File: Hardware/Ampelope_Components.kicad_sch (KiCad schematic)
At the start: 121 parts, among them J1 Conn_01x12_Male, J2 Conn_01x12_Male, J3 Conn_01x12_Male, J4 Conn_01x12_Male, J5 Eurorack_16_pin_power, J6 Conn_01x02_Male, J7 SWD_Header, J8 USB_B_Micro, J9 Conn_01x02_Male, Q1 MMBT3906, Q2 MMBT3906, Q3 MMBT3906, Q4 MMBT3906, Q5 MMBT3906, U1 STM32G431RB, U2 AS3364, U3 LM1117-3.3, U4 TL074, U5 TL074, U6 TL074, Y1 8MHz 20pF

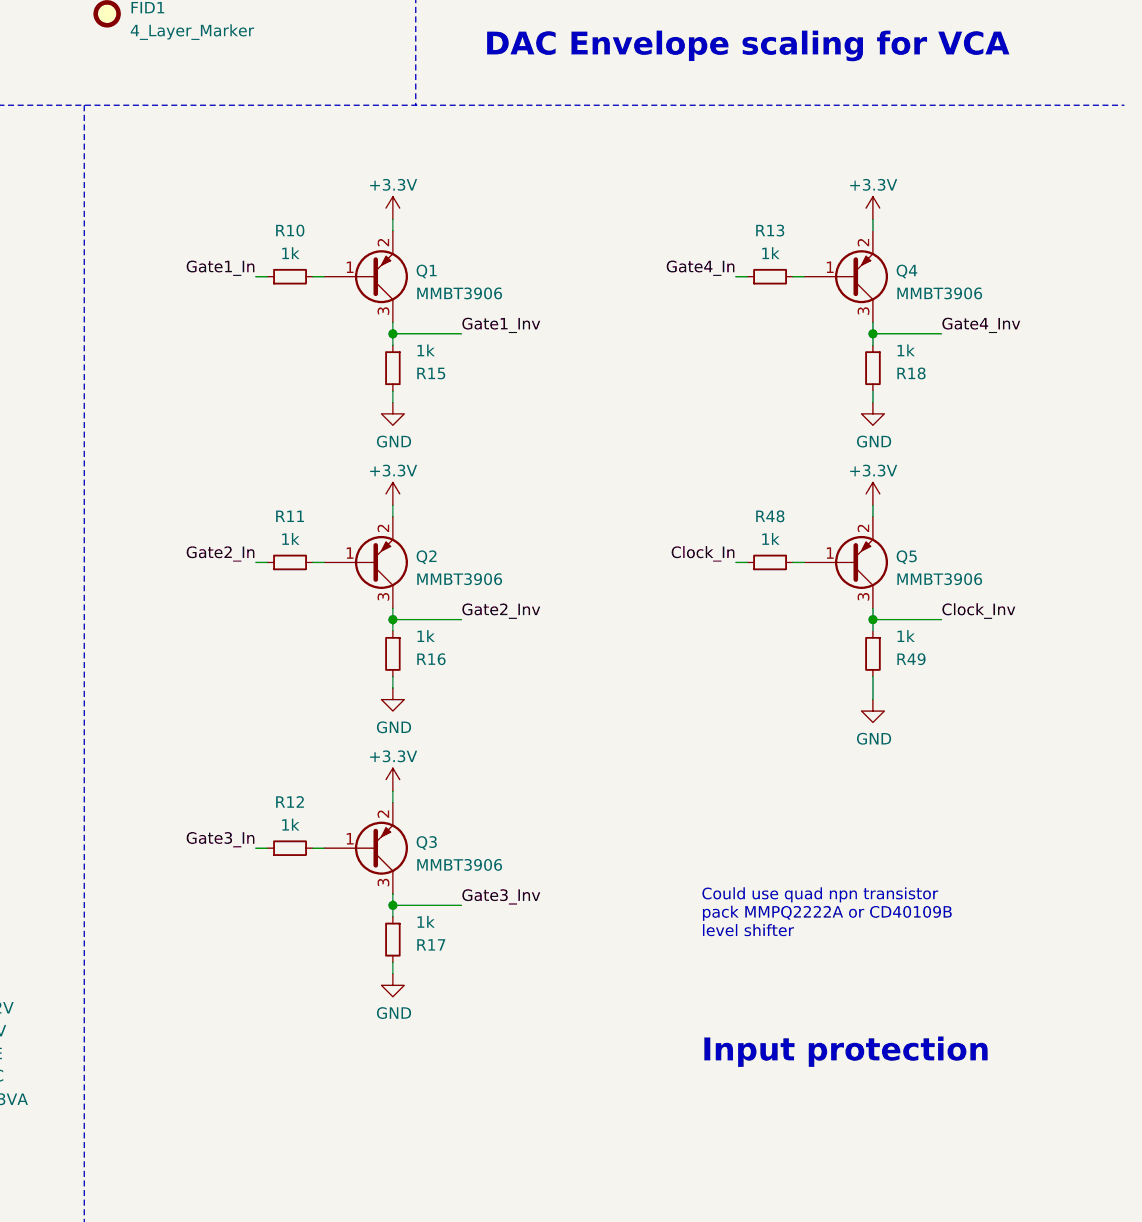
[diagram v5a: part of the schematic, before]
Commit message: Changed input protection diodes back to 3904s; prepared gerbers
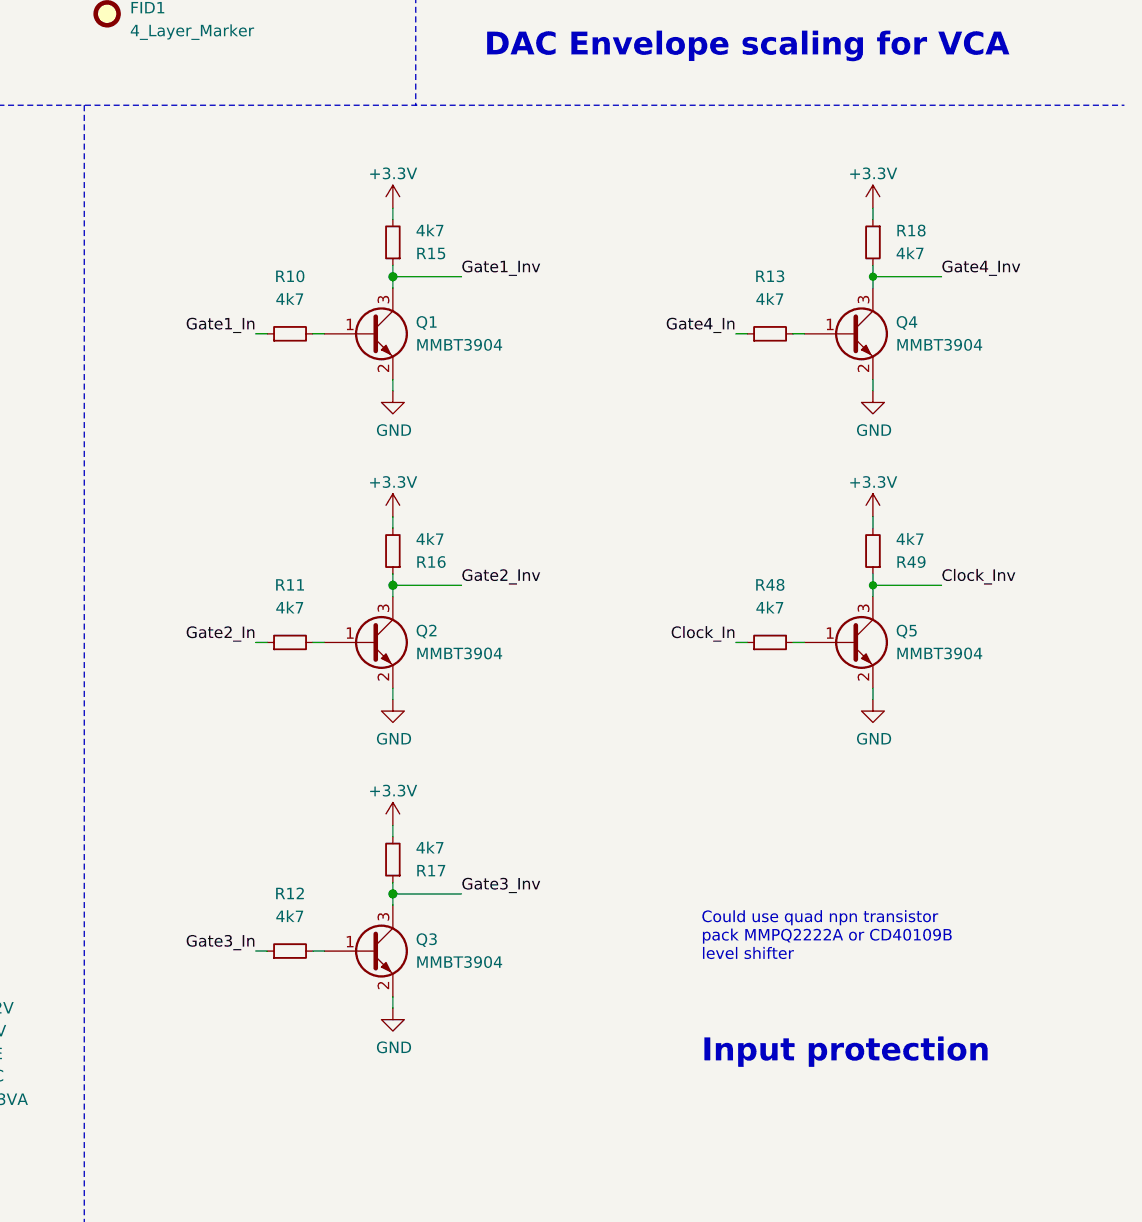
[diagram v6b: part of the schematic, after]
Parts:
- removed Q1, Q2, Q3, Q4, Q5: MMBT3906, Package_TO_SOT_SMD:SOT-23, symbol Transistor_BJT:MMBT3906
- added Q1, Q2, Q3, Q4, Q5: MMBT3904, Package_TO_SOT_SMD:SOT-23, symbol Transistor_BJT:MMBT3904
- C10: Part_Number (none) -> C19666
- C11, C13, C23, C26, C9: Part_Number (none) -> C14663
- C12, C15: Part_Number (none) -> C15849
- C14: Part_Number (none) -> C57112
- C16, C17, C18, C19: Part_Number C84721 -> (none)
- C21, C22: Part_Number C84721 -> C14663
- C24, C25: Part_Number (none) -> C22397
- C27, C28, C29, C30: Part_Number C57112 -> C1604
- C5, C6, C7, C8: Part_Number (none) -> C14858
- L1: Part_Number (none) -> C1046
- R1, R3, R5, R7: Part_Number C22984 -> C21190
- R10, R11, R12, R13, R15, R16, R17, R18, R48, R49: value 1k -> 4k7; Part_Number (none) -> C23162
- R19, R20, R21, R22, R23, R24, R25, R26: Part_Number C22984 -> C25804
- R35, R37, R39, R41: Part_Number (none) -> C23212
- R36, R38, R40, R42: Part_Number C25803 -> C22978
- R43, R44, R45, R46: Part_Number C25819 -> C23162
- R47, R50, R51, R52, R57, R58, R59, R60: Part_Number C25819 -> C21190
- R53, R54, R55, R56: Part_Number (none) -> C25804
- R9: Part_Number (none) -> C25803
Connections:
- net +3V3: now also R15.2, R16.2, R17.2, R18.1, R49.2
- net Clock_Inv: now also Q5.3 (C)
- net GND: now also Q1.2 (E), Q2.2 (E), Q3.2 (E), Q4.2 (E), Q5.2 (E); no longer R15.2, R16.2, R17.2, R18.2, R49.2
- net Gate1_Inv: now also Q1.3 (C)
- net Gate2_Inv: now also Q2.3 (C)
- net Gate3_Inv: now also Q3.3 (C)
- net Gate4_Inv: now also R18.2, Q4.3 (C); no longer R18.1
- net at R12.2: now also Q3.1 (B)
- net at R10.2: now also Q1.1 (B)
- net at R48.2: now also Q5.1 (B)
- net at R11.2: now also Q2.1 (B)
- net at R13.2: now also Q4.1 (B)
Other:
- moved on the sheet: R10, R11, R12, R13, R15, R16, R17, R18, R48, R49

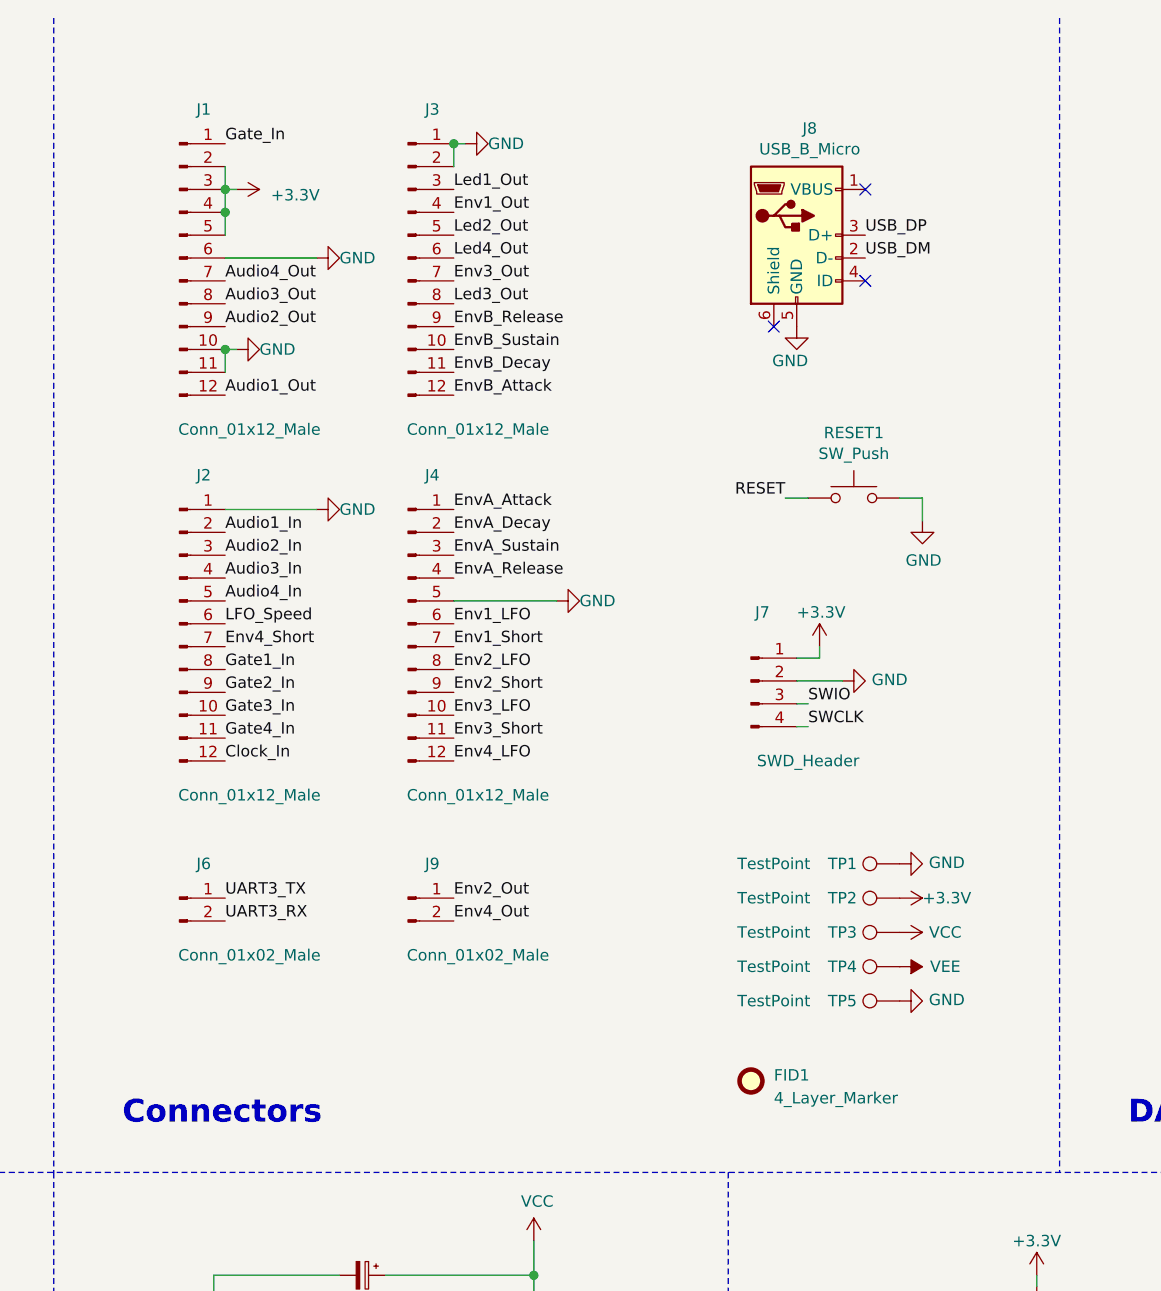
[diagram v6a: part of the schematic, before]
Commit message: Prepared gerbers for pcb manufacture
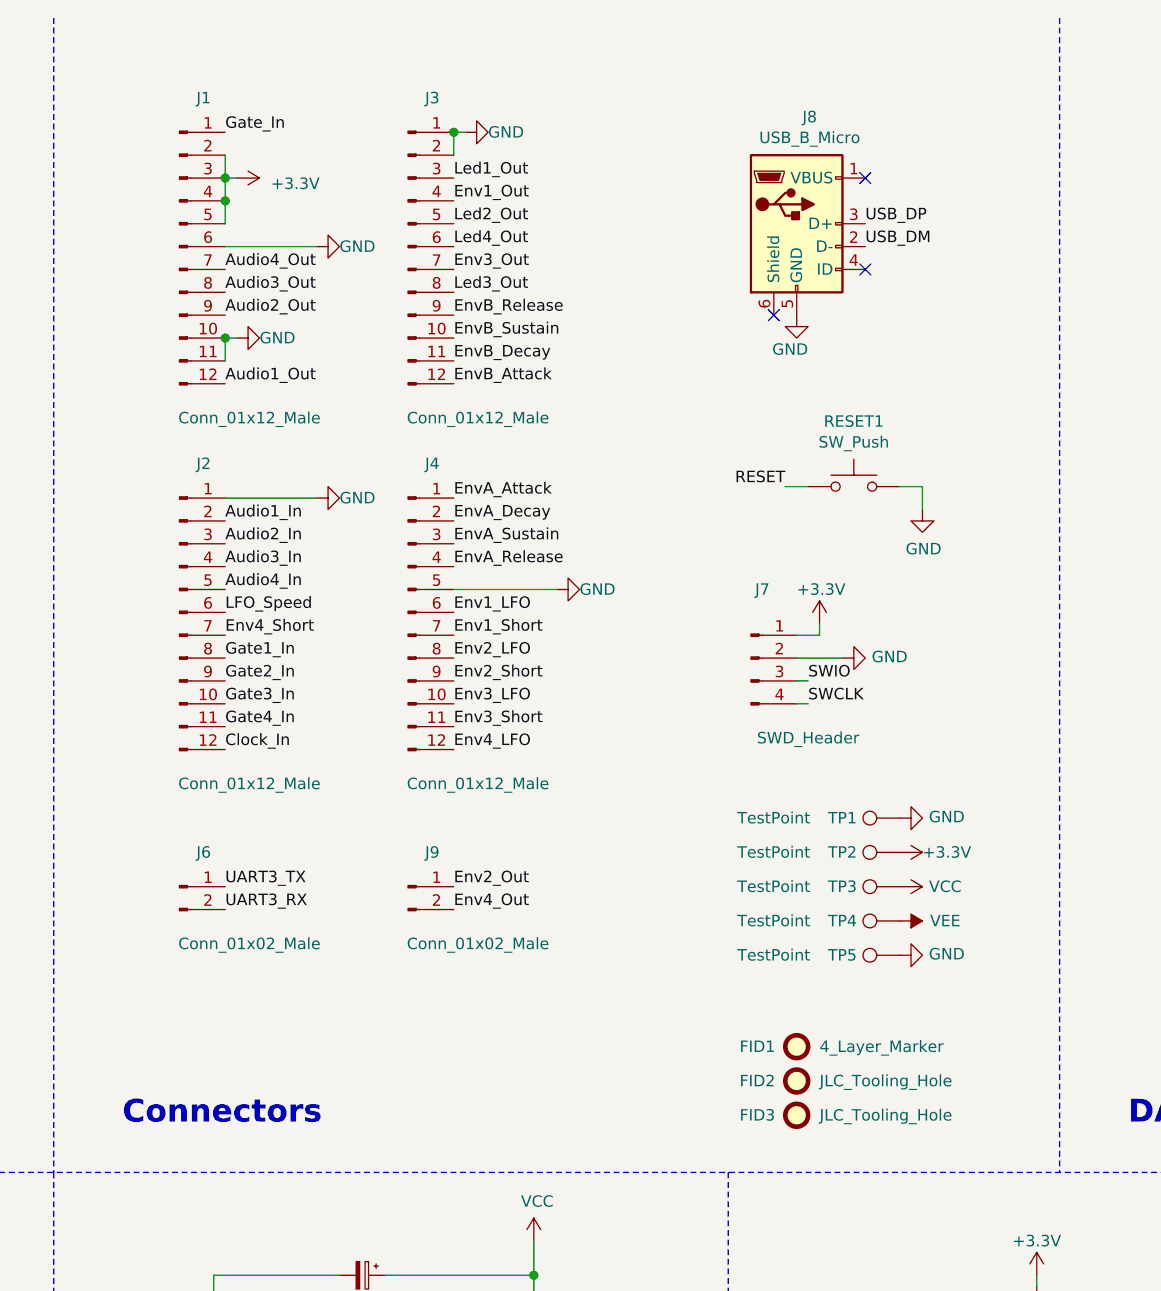
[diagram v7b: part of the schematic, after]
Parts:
- added FID2, FID3: JLC_Tooling_Hole, Custom_Footprints:JLC_SMT_Tooling_Hole, symbol Mechanical:Fiducial
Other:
- moved on the sheet: FID1, J1, J2, J3, J4, J6, J7, J8, J9, RESET1, TP1, TP2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

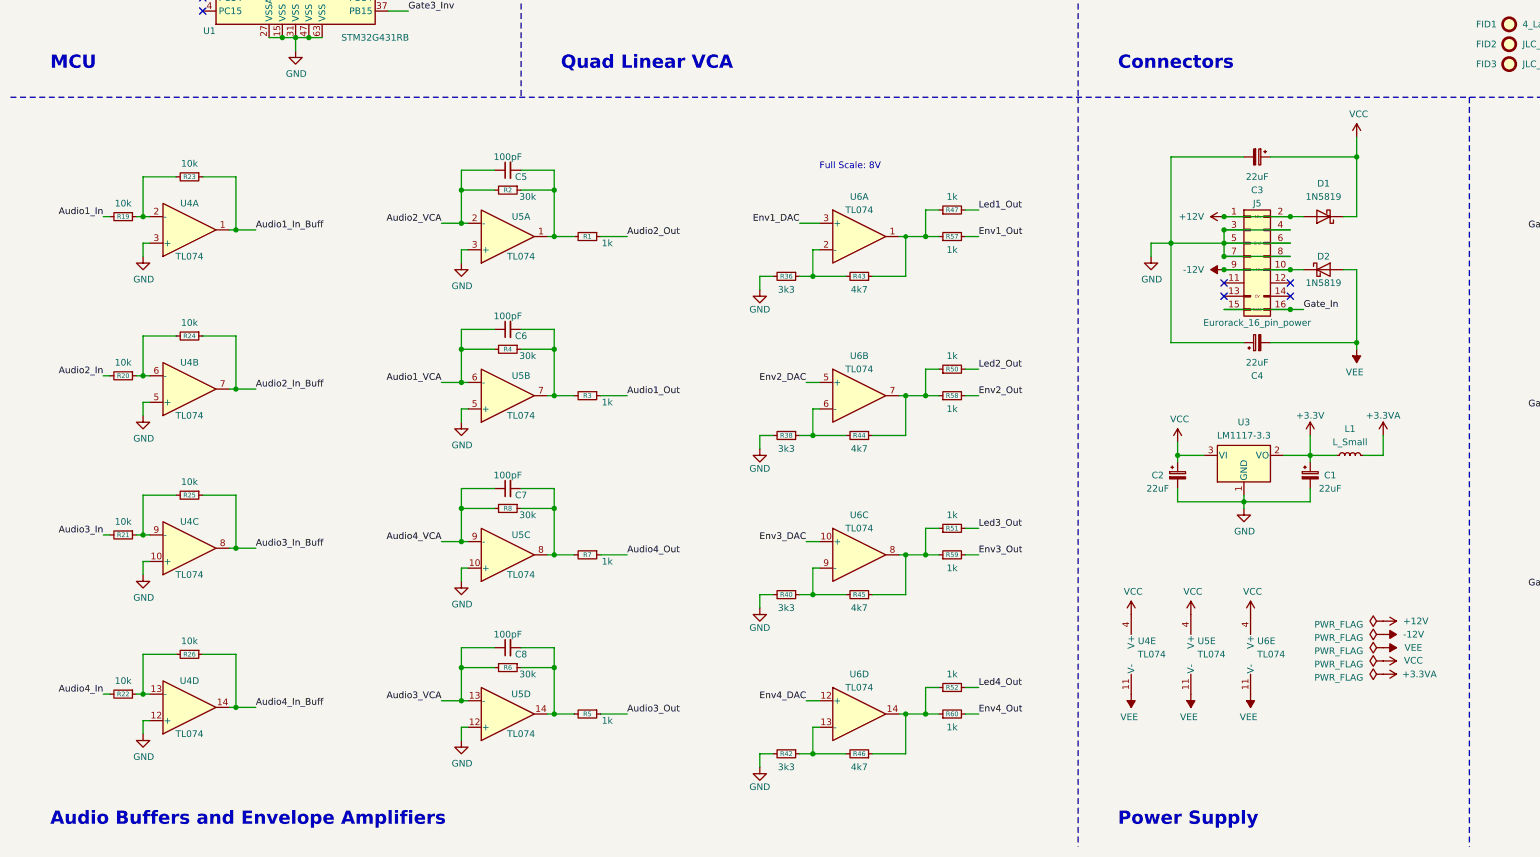
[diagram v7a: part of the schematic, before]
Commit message: Fixes to component schematic and pcb (power supply and silkscreen); Firmware updated to use correct pin assignments
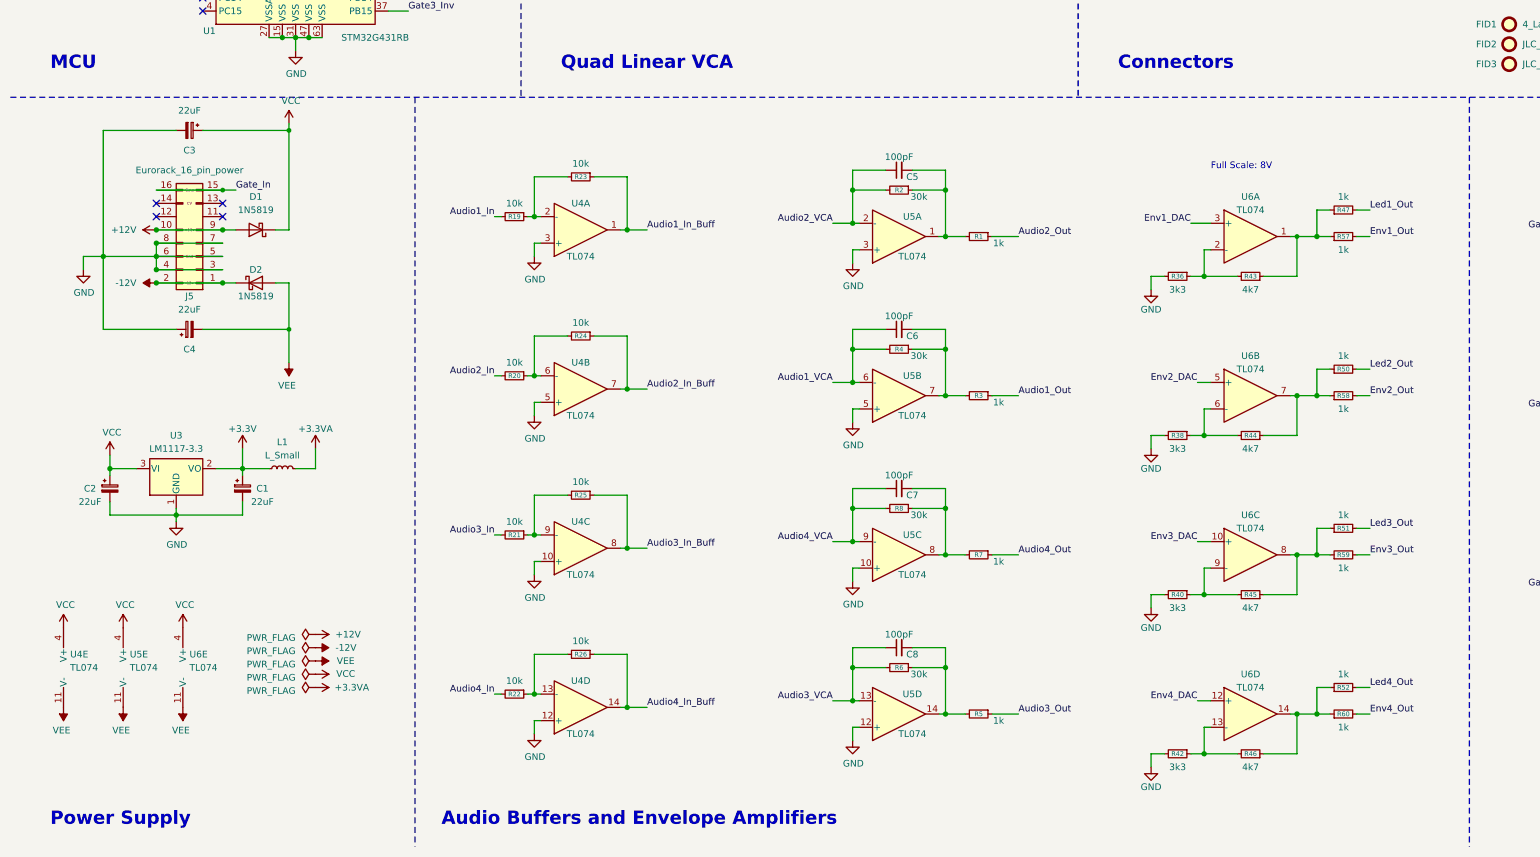
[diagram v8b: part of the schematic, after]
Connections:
- net +12V: now also J5.10 (Pin_10), J5.9 (Pin_9); no longer J5.1 (Pin_1), J5.2 (Pin_2)
- net -12V: now also J5.1 (Pin_1), J5.2 (Pin_2); no longer J5.10 (Pin_10), J5.9 (Pin_9)
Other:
- moved on the sheet: C1, C2, C3, C4, C5, C6, C7, C8, D1, D2, J5, L1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
